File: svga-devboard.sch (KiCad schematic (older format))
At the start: 40 parts, among them J1 Bus_PCI_32bit_Universal, U1 SN74LVCH16T245DGGR, U2 SN74LVCH16T245DGGR, U3 SN74LVCH16T245DGGR, U4 SN74LVCH16T245DGGR, U5 SN74LVCH16T245DGGR

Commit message: Add files via upload
Converted to hierarchical scheets, added support-components for SMPS-units - many other changes.
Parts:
- removed C1-1, C1-2, C1-3, C2-1, C2-2, C2-3: 22UF-1206-16V-10%, Capacitor_SMD:C_1206_3216Metric_Pad1.42x1.75mm_HandSolder, symbol LRJ-parts:22UF-1206-16V-10%
- removed DDR4: AS4C256M16D4-75BCN, Package_BGA:FBGA-96-Alliance_, symbol LRJ-parts:AS4C256M16D4-75BCN
- removed DVI1: 74320-9010, digikey-footprints:DVI_Female_74320-9010, symbol dk_USB-DVI-HDMI-Connectors:74320-9010
- removed FPGA1: LFE5U-85F-BG381, Package_BGA:caBGA-381_15.2x15.2_17.0x17.0mm, symbol svga-devboard-rescue:LFE5U-85F-BG381-LRJ-parts-svga-devboard-rescue
- removed J1: Bus_PCI_32bit_Universal, Connector_PCBEdge:BUS_PCI_UNI_32-lrj, symbol Connector:Bus_PCI_32bit_Universal
- removed L1-1, L1-2, L1-3, L2-1, L2-2, L2-3: 1008PS-102KLC, Inductor_SMD:L_1008_2520Metric, symbol LRJ-parts:1008PS-102KLC
- removed R1-1, R1-2, R1-3, R2-1, R2-2, R2-3: CRCW12064R99FKEAHP, Resistor_SMD:R_1206_3216Metric_Pad1.42x1.75mm_HandSolder, symbol LRJ-parts:CRCW12064R99FKEAHP
- removed R3-1, R3-2, R3-3, R4-1, R4-2, R4-3: CMP2010-FX-1002ELF, Resistor_SMD:R_2010_5025Metric_Pad1.52x2.65mm_HandSolder, symbol LRJ-parts:CMP2010-FX-1002ELF
- removed R50: TE_CGS_SMF52M0JT_1MOHM-_5W-5%, Resistor_SMD:TE_CGS_SMF52M0JT_Pad3.4x4.5mm, symbol LRJ-parts:TE_CGS_SMF52M0JT_1MOHM-_5W-5%
- removed SMP1, SMP2, SMP3: LM26420-Q1MHX_NOPB, Package_SO:HTSSOP-20-1EP_4.4x6.5mm_P0.42mm_EP3.2x6.4mm_Mask3.0x4.2mm_ThermalVias, symbol Regulator_Switching:LM26420-Q1MHX_NOPB
- removed U1, U2, U3, U4, U5: SN74LVCH16T245DGGR, Package_SO:TSSOP-48_6.1x12.5mm_P0.5mm, symbol LRJ-parts:SN74LVCH16T245DGGR
- removed USB1: USB_C_Amphenol_10133476-10001LF, Connector_USB:USB-C_Female_10133476-10001LF, symbol Connector:USB_C_Amphenol_10133476-10001LF
- removed VBIOS1: Cypress_Semi_S25FL128LAGMFV013, Package_SO:Cypress_Semi_S25FL128LAGMFV013, symbol LRJ-parts:Cypress_Semi_S25FL128LAGMFV013
- removed VGA1: Amphenol_L77HDE15SD1CH4RHNVGA, Connector_Dsub:DSUB-Amphenol_L77HDE15SD1CH4RHNVGA, symbol Connector:Amphenol_L77HDE15SD1CH4RHNVGA
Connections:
- net labels removed: +12V, +3.3V, +5V, -12V, 0.8V2, 1.1V1, 1.1V2, 1.2V1, 1.8V1, 2.5V1, 66M, A-0, A-02, A-03, A-04, A-05, A-06, A-07, A-08, A-09, A-1, A-10, A-11, A-12, A-13, A-14, A-15, A-16, A-17, A-18, A-19, A-20, A-21, A-22, A-23, A-24, A-25, A-26, A-27, A-28, A-29, A-30, A-31, A-32, A-33, A-34, A-35, A-36, A-37, A-38, A-39, A-40, A-41, A-42, A-43, A-44, A-45, A-46, A-47, A-48, A-49, A-50, A-51, A-52, A-53, A-54, A-55, A-56, A-57, A-58, A-59, A-60, A-61, A-62, A-63, AC6-, AC64, ADBC, ADBC-1, ADBC-10, ADBC-12, ADBC-14, ADBC-17, ADBC-19, ADBC-21, ADBC-23, ADBC-25, ADBC-27, ADBC-29, ADBC-3, ADBC-31, ADBC-5, ADBC-7, ADBC-8, ADBS, ADBS-0, ADBS-11, ADBS-13, ADBS-15, ADBS-16, ADBS-18, ADBS-2, ADBS-20, ADBS-22, ADBS-24, ADBS-26, ADBS-28, ADBS-30, ADBS-4, ADBS-6, ADBS-9, CBE0, CBE0_, CBE1, CBE2, CBE3, CBE4, CBE5, CBE6, CBE7, CB_2, CB_4, CB_5, CB_6, CB_7, CLK, CLK_, CSv, DEVSEL, DVSL, FRAME, FRME, GND, GNDA, GNT, GNT_, IDSEL, INTA, INTA_, INTB, INTB_, INTC, INTC_, INTD, INTD_, IRDY, IRD_, LOCK, LOC_, M66E, MCBC, MCBS, PAR, PAR_, PERR, PER_, PME, PME_, PRSNT1, PRSNT2, PRSN_1, PRSN_2, REQ, REQ64, REQ_, RQ64, RST, RST_, RSTv, SCKv, SCLK, SDAT, SERR, SER_, SI, SMCLK, SMDAT, SO, STOP, STO_, SVR1_B, SVR2_B, SVR3_B, TCLK, TCLK_, TDI, TDI_, TDO, TDO_, TMS, TMS_, TRDY, TRD_, TRST, TRST_, VTA, VTB, VTM, WP, XCAP, XCA_
- wire segments 1032 -> 0
- no-connect marks 17 -> 0
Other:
- note added: "PCI BUS"
- note added: "PCI_ADb = ADress bus pci B-side (top)\nPCI_ADa = ADress bus pci A-side (bottom)"
- note added: "PCI_MB = Miscellaneous signals PCI bus B-side (top)\nPCI_MA= Miscellaneous signals PCI bus A-side (bottom)"
- note added: "PCI_VTA = PCI Voltage Translated Adressing\nPCI_VTM = PCI Voltage Translated bus Miscellaneous signals"
- note added: "POWER"
- note added: "SMPS = Switched Mode Power supply"
- note added: "Signal Voltage Level Translation"
- note removed: "0.8V out"
- note removed: "1.1V"
- note removed: "1.1V out"
- note removed: "1.8V out"
- note removed: "2.5V"
- note removed: "2.5V & 1.2 Supply\n"
- note removed: "2.5V Out"
- note removed: "3.3V converter\n"
- note removed: "5V converter\n"
- note removed: "ADBC = ADress Bus pci C-side (top)\nADBS = ADress Bus pci S-side (bottom)"
- note removed: "Analogue Ground"
- note removed: "MCBC = MisCellaneous Bus C-side (top)\nMCBS = MisCellaneous Bus S-side (bottom)"
- note removed: "SMP = Switched Mode Power supply"
- note removed: "VTA = Voltage Translated Adressing\nVTM = Voltage Translated Bus Miscellaneous"

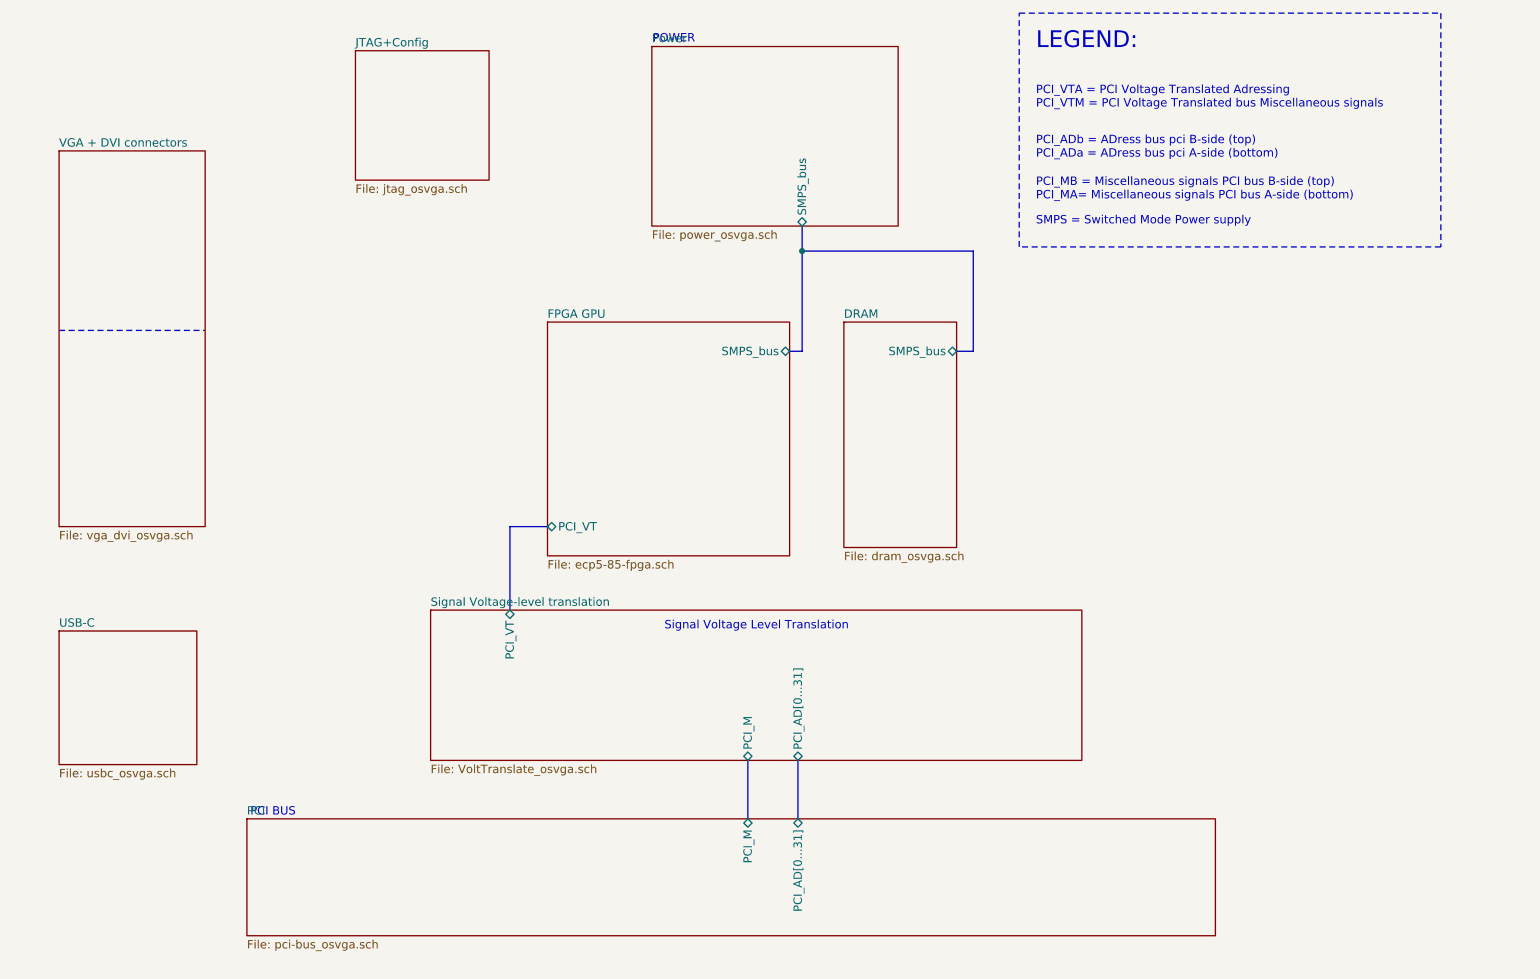
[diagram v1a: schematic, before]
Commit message: Add files via upload
Added Pull-up and pull-down resistors for JTAG and sysConfig connections.
Added pinheaders for FPGA-Configuration. (replacing edge-connector)
Combined the DVI+VGA and USB-C hierarchical sheets into one.
Assigned a dedicated sheet for the DAC.
Added 75 Ohm terminal-resistors to output of DAC.
Placed filtering-capacitors for DAC VAA.
Connected VGA ID-bits and DVI DDC together.
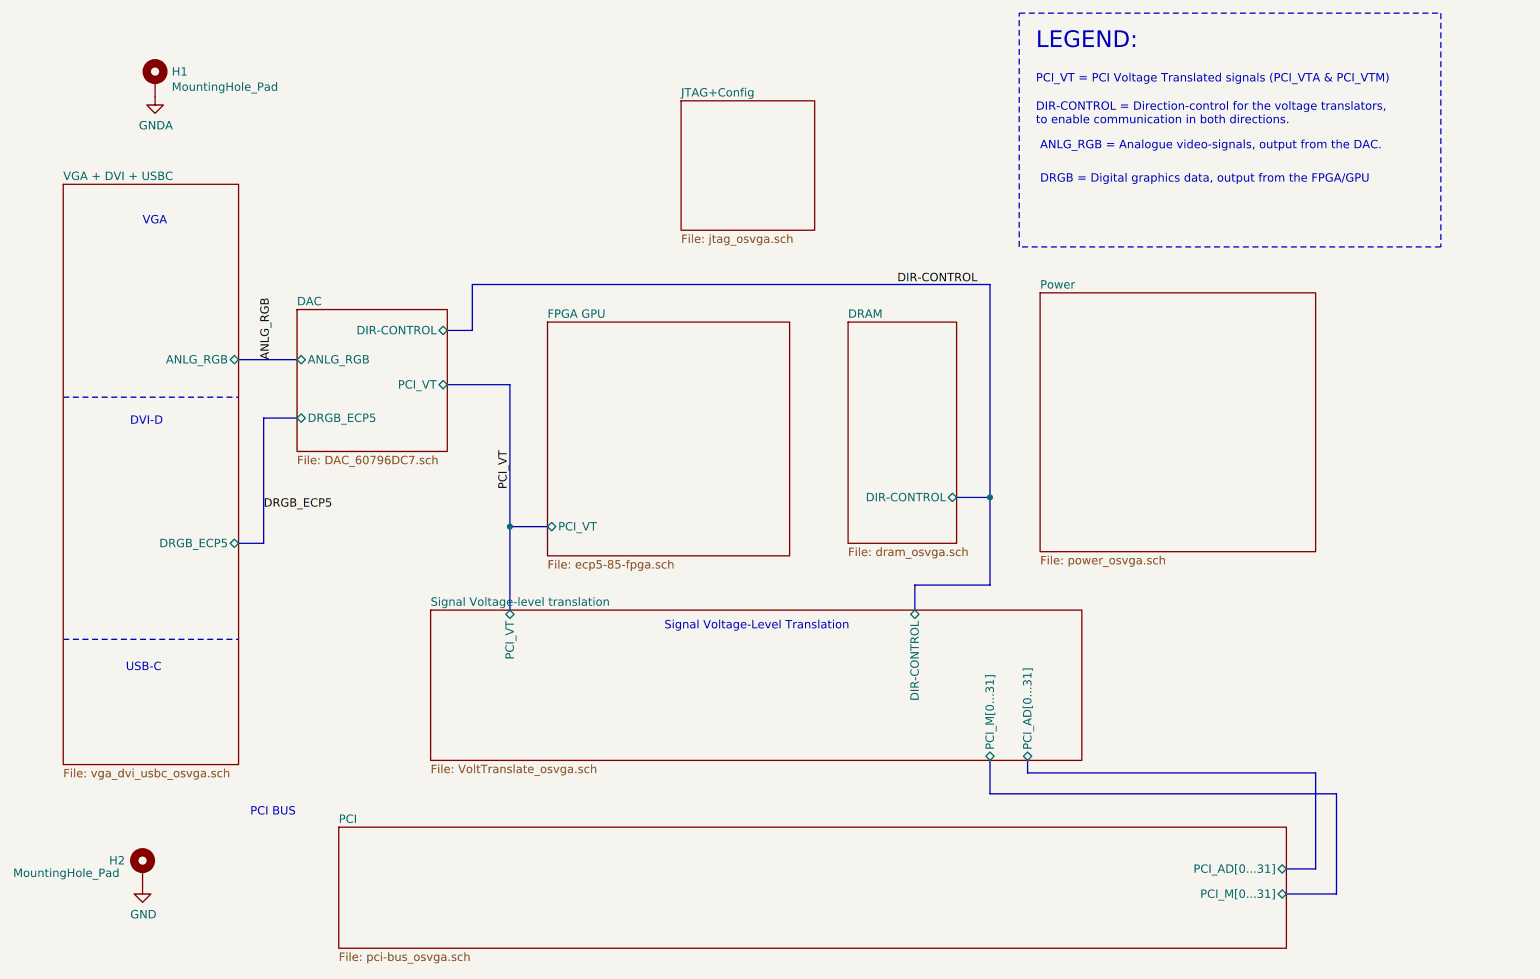
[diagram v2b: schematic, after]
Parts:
- added H1, H2: MountingHole_Pad, MountingHole:MountingHole_3.2mm_M3_Pad_Via, symbol Mechanical:MountingHole_Pad
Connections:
- new net GND: H2.1
- new net GNDA: H1.1
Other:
- note added: "ANLG_RGB = Analogue video-signals, output from the DAC."
- note added: "DIR-CONTROL = Direction-control for the voltage translators, \nto enable communication in both directions."
- note added: "DRGB = Digital graphics data, output from the FPGA/GPU"
- note added: "DVI-D"
- note added: "PCI_VT = PCI Voltage Translated signals (PCI_VTA & PCI_VTM)"
- note added: "Signal Voltage-Level Translation"
- note added: "USB-C"
- note added: "VGA"
- note removed: "PCI_ADb = ADress bus pci B-side (top)\nPCI_ADa = ADress bus pci A-side (bottom)"
- note removed: "PCI_MB = Miscellaneous signals PCI bus B-side (top)\nPCI_MA= Miscellaneous signals PCI bus A-side (bottom)"
- note removed: "PCI_VTA = PCI Voltage Translated Adressing\nPCI_VTM = PCI Voltage Translated bus Miscellaneous signals"
- note removed: "POWER"
- note removed: "SMPS = Switched Mode Power supply"
- note removed: "Signal Voltage Level Translation"
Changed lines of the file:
@@
 	10900 725  10900 2125
 $Sheet
-S 3750 5550 5800 700
-U 6666DF7A
-F0 "PCI" 50
-F1 "pci-bus_osvga.sch" 50
-F2 "PCI_AD[0...31]" B T 7050 5550 50
-F3 "PCI_M" B T 6750 5550 50
-$EndSheet
-$Sheet
-S 4400 950  800  775
+S 6350 1250 800  775
 U 5F5F9E24
 F0 "JTAG+Config" 50
@@
 Wire Notes Line
 	8375 725  10900 725
+Text Notes 8475 1400 0    50   ~ 0
+DIR-CONTROL = Direction-control for the voltage translators, \nto enable communication in both directions.
+Text Notes 8475 1150 0    50   ~ 0
+PCI_VT = PCI Voltage Translated signals (PCI_VTA & PCI_VTM)
+Text Notes 8475 950  0    100  ~ 0
+LEGEND:
+Text Notes 6250 4425 0    50   ~ 0
+Signal Voltage-Level Translation
+Text Notes 3770 5540 0    50   ~ 0
+PCI BUS
 $Sheet
-S 7325 2575 675  1350
+S 7350 2575 650  1325
 U 649752B2
 F0 "DRAM" 50
 F1 "dram_osvga.sch" 50
-F2 "SMPS_bus" B R 8000 2750 50
+F2 "DIR-CONTROL" B R 8000 3625 50
 $EndSheet
-Text Notes 8475 2000 0    50   ~ 0
-SMPS = Switched Mode Power supply
-Text Notes 8475 1850 0    50   ~ 0
-PCI_MB = Miscellaneous signals PCI bus B-side (top)\nPCI_MA= Miscellaneous signals PCI bus A-side (bottom)
-Text Notes 8475 1600 0    50   ~ 0
-PCI_ADb = ADress bus pci B-side (top)\nPCI_ADa = ADress bus pci A-side (bottom)
-Text Notes 8475 1300 0    50   ~ 0
-PCI_VTA = PCI Voltage Translated Adressing\nPCI_VTM = PCI Voltage Translated bus Miscellaneous signals
-Text Notes 8475 950  0    100  ~ 0
-LEGEND:
+$Sheet
+S 2650 1750 1050 3475
+U 629A7666
+F0 "VGA + DVI + USBC" 50
+F1 "vga_dvi_usbc_osvga.sch" 50
+F2 "ANLG_RGB" B R 3700 2800 50
+F3 "DRGB_ECP5" B R 3700 3900 50
+$EndSheet
+$Sheet
+S 8500 2400 1650 1550
+U 652C62BE
+F0 "Power" 50
+F1 "power_osvga.sch" 50
+$EndSheet
+Wire Notes Line
+	2650 4475 3700 4475
+Wire Notes Line
+	2650 3025 3700 3025
+Text Notes 3025 4675 0    50   ~ 0
+USB-C
+Text Notes 3050 3200 0    50   ~ 0
+DVI-D
+Text Notes 3125 2000 0    50   ~ 0
+VGA
 Wire Bus Line
-	7050 5550 7050 5200
+	5325 3800 5550 3800
+$Sheet
+S 5550 2575 1450 1400
+U 5F777FFB
+F0 "FPGA GPU" 50
+F1 "ecp5-85-fpga.sch" 50
+F2 "PCI_VT" B L 5550 3800 50
+$EndSheet
+$Sheet
+S 4050 2500 900  850
+U 60796DC8
+F0 "DAC" 50
+F1 "DAC_60796DC7.sch" 50
+F2 "DRGB_ECP5" B L 4050 3150 50
+F3 "ANLG_RGB" B L 4050 2800 50
+F4 "PCI_VT" B R 4950 2950 50
+F5 "DIR-CONTROL" B R 4950 2625 50
+$EndSheet
 Wire Bus Line
-	6750 5550 6750 5200
+	3700 3900 3850 3900
+Wire Bus Line
+	3850 3900 3850 3150
+Wire Bus Line
+	3850 3150 4050 3150
+Wire Bus Line
+	3700 2800 4050 2800
+$Comp
+L Mechanical:MountingHole_Pad H2
+U 1 1 61D70614
+P 3125 5850
+F 0 "H2" H 2925 5900 50  0000 L CNN
+F 1 "MountingHole_Pad" H 2350 5825 50  0000 L CNN
+F 2 "MountingHole:MountingHole_3.2mm_M3_Pad_Via" H 3125 5850 50  0001 C CNN
+F 3 "~" H 3125 5850 50  0001 C CNN
+	1    3125 5850
+	1    0    0    -1
+$EndComp
+$Comp
+L power:GND #PWR0104
+U 1 1 61D75C03
+P 3125 5950
+F 0 "#PWR0104" H 3125 5700 50  0001 C CNN
+F 1 "GND" H 3130 5777 50  0000 C CNN
+F 2 "" H 3125 5950 50  0001 C CNN
+F 3 "" H 3125 5950 50  0001 C CNN
+	1    3125 5950
+	1    0    0    -1
+$EndComp
+$Comp
+L power:GNDA #PWR0189
+U 1 1 61D76331
+P 3200 1225
+F 0 "#PWR0189" H 3200 975 50  0001 C CNN
+F 1 "GNDA" H 3205 1052 50  0000 C CNN
+F 2 "" H 3200 1225 50  0001 C CNN
+F 3 "" H 3200 1225 50  0001 C CNN
+	1    3200 1225
+	1    0    0    -1
+$EndComp
+$Comp
+L Mechanical:MountingHole_Pad H1
+U 1 1 61D6F266
+P 3200 1125
+F 0 "H1" H 3300 1174 50  0000 L CNN
+F 1 "MountingHole_Pad" H 3300 1083 50  0000 L CNN
+F 2 "MountingHole:MountingHole_3.2mm_M3_Pad_Via" H 3200 1125 50  0001 C CNN
+F 3 "~" H 3200 1125 50  0001 C CNN
+	1    3200 1125
+	1    0    0    -1
+$EndComp
+Wire Bus Line
+	5325 3800 5325 4300
+Wire Bus Line
+	5325 3800 5325 2950
+Wire Bus Line
+	5325 2950 4950 2950
+Connection ~ 5325 3800
+Wire Bus Line
+	7750 4300 7750 4150
+Wire Bus Line
+	7750 4150 8200 4150
+Wire Bus Line
+	8200 4150 8200 3625
+Wire Bus Line
+	8200 3625 8000 3625
+Wire Bus Line
+	8200 3625 8200 2350
+Wire Bus Line
+	8200 2350 5100 2350
+Connection ~ 8200 3625
+Wire Bus Line
+	5100 2350 5100 2625
+Wire Bus Line
+	5100 2625 4950 2625
+Text Notes 8500 1550 0    50   ~ 0
+ANLG_RGB = Analogue video-signals, output from the DAC.
+Text Notes 8500 1750 0    50   ~ 0
+DRGB = Digital graphics data, output from the FPGA/GPU
 $Sheet
 S 4850 4300 3900 900
@@
 F0 "Signal Voltage-level translation" 50
 F1 "VoltTranslate_osvga.sch" 50
-F2 "PCI_M" B B 6750 5200 50
-F3 "PCI_AD[0...31]" B B 7050 5200 50
-F4 "PCI_VT" B T 5325 4300 50
-$EndSheet
-Wire Notes Line
-	2625 2625 3500 2625
-$Sheet
-S 2625 1550 875  2250
-U 629A7666
-F0 "VGA + DVI connectors" 50
-F1 "vga_dvi_osvga.sch" 50
+F2 "PCI_VT" B T 5325 4300 50
+F3 "DIR-CONTROL" B T 7750 4300 50
+F4 "PCI_AD[0...31]" B B 8425 5200 50
+F5 "PCI_M[0...31]" B B 8200 5200 50
 $EndSheet
 $Sheet
-S 6175 925  1475 1075
-U 652C62BE
-F0 "Power" 50
-F1 "power_osvga.sch" 50
-F2 "SMPS_bus" B B 7075 2000 50
+S 4300 5600 5675 725
+U 6666DF7A
+F0 "PCI" 50
+F1 "pci-bus_osvga.sch" 50
+F2 "PCI_AD[0...31]" B R 9975 5850 50
+F3 "PCI_M[0...31]" B R 9975 6000 50
 $EndSheet
+Text Label 8125 2350 2    50   ~ 0
+DIR-CONTROL
+Text Label 5325 3575 1    50   ~ 0
+PCI_VT
+Text Label 3850 3700 0    50   ~ 0
+DRGB_ECP5
+Text Label 3900 2800 1    50   ~ 0
+ANLG_RGB
 Wire Bus Line
-	7075 2000 7075 2150
-$Sheet
-S 5550 2575 1450 1400
-U 5F777FFB
-F0 "FPGA GPU" 50
-F1 "ecp5-85-fpga.sch" 50
-F2 "SMPS_bus" B R 7000 2750 50
-F3 "PCI_VT" B L 5550 3800 50
-$EndSheet
+	9975 5850 10150 5850
 Wire Bus Line
-	7075 2150 8100 2150
+	10150 5850 10150 5275
 Wire Bus Line
-	8100 2150 8100 2750
+	10150 5275 8425 5275
 Wire Bus Line
-	8100 2750 8000 2750
+	8425 5275 8425 5200
 Wire Bus Line
-	7000 2750 7075 2750
+	9975 6000 10275 6000
 Wire Bus Line
-	7075 2750 7075 2150
-Connection ~ 7075 2150
+	10275 6000 10275 5400
 Wire Bus Line
-	5325 4300 5325 3800
+	10275 5400 8200 5400
 Wire Bus Line
-	5325 3800 5550 3800
-$Sheet
-S 2625 4425 825  800
-U 629BDEA3
-F0 "USB-C" 50
-F1 "usbc_osvga.sch" 50
-$EndSheet
-Text Notes 6180 910  0    50   ~ 0
-POWER
-Text Notes 6250 4425 0    50   ~ 0
-Signal Voltage Level Translation
-Text Notes 3770 5540 0    50   ~ 0
-PCI BUS
+	8200 5400 8200 5200
 $EndSCHEMATC
